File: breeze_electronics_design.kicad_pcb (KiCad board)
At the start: 2 copper layers, 104.1 x 104.1 mm, 104 parts, among them J1 SIP4, M1 MotorA, M2 MotorB, M3 MotorA, M4 MotorB, Q1 S8050, Q2 SI2302, Q3 SI2302, Q4 SI2302, Q5 SI2302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

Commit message: Finish the basic check of layout
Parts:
- removed the ? at (-94.9, -94.9)
- removed the ? at (-94.9, -5.08)
- removed the ? at (-5.08, -5.08)
- removed the ? at (-5.08, -94.9)
- added ?: , Footprint:PTH_Motor, F.Cu at (5.08, -94.9)
- added ?: Motor, Footprint:PTH_Motor, F.Cu at (94.9, -5.08)
- added ?: Motor, Footprint:PTH_Motor, F.Cu at (94.9, -94.9)
- added ?: Motor, Footprint:PTH_Motor, F.Cu at (5.08, -5.08)
- added REF**: LOGO_Arrow, Footprint:LOGO_Arrow, F.Cu at (50.0, -54.1)
- added REF**: LOGO_Project, Footprint:LOGO_Project, F.Cu at (64.5, -31.0)
- added REF***: OSHW-Logo_5.7x6mm_SilkScreen, Symbols:OSHW-Logo_5.7x6mm_SilkScreen, F.Cu at (57.4, -29.7)
- H1, LED3, LED5, LED7, LED9, M1, M2, M3, M4, USB1: moved to B.Cu
- S1: footprint Footprint:DIP_SW2x3 -> DIP_SW2x3
- moved C7 109.5 mm to (67.1, -43.4)
- moved LED6 102.6 mm to (77.5, -22.6)
- moved M4 101.6 mm to (81.3, -79.8)
- moved M1 101.5 mm to (20.3, -81.3)
- moved C6 100.6 mm to (55.4, -58.2)
- moved C9 100.6 mm to (55.4, -63.0)
- moved C4 100.3 mm to (69.3, -55.1)
- moved U5 100.3 mm to (58.9, -37.6)
- moved C16 100.3 mm to (36.8, -48.0)
- moved C3 100.3 mm to (50.0, -58.2)
- moved R14 100.3 mm to (30.5, -58.2)
- moved R2 100.3 mm to (50.0, -67.1)
- moved R3 100.3 mm to (50.0, -62.7)
- moved C24 100.1 mm to (27.4, -51.6)
- moved Y1 100.1 mm to (57.7, -51.6), turned to 270 degrees
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
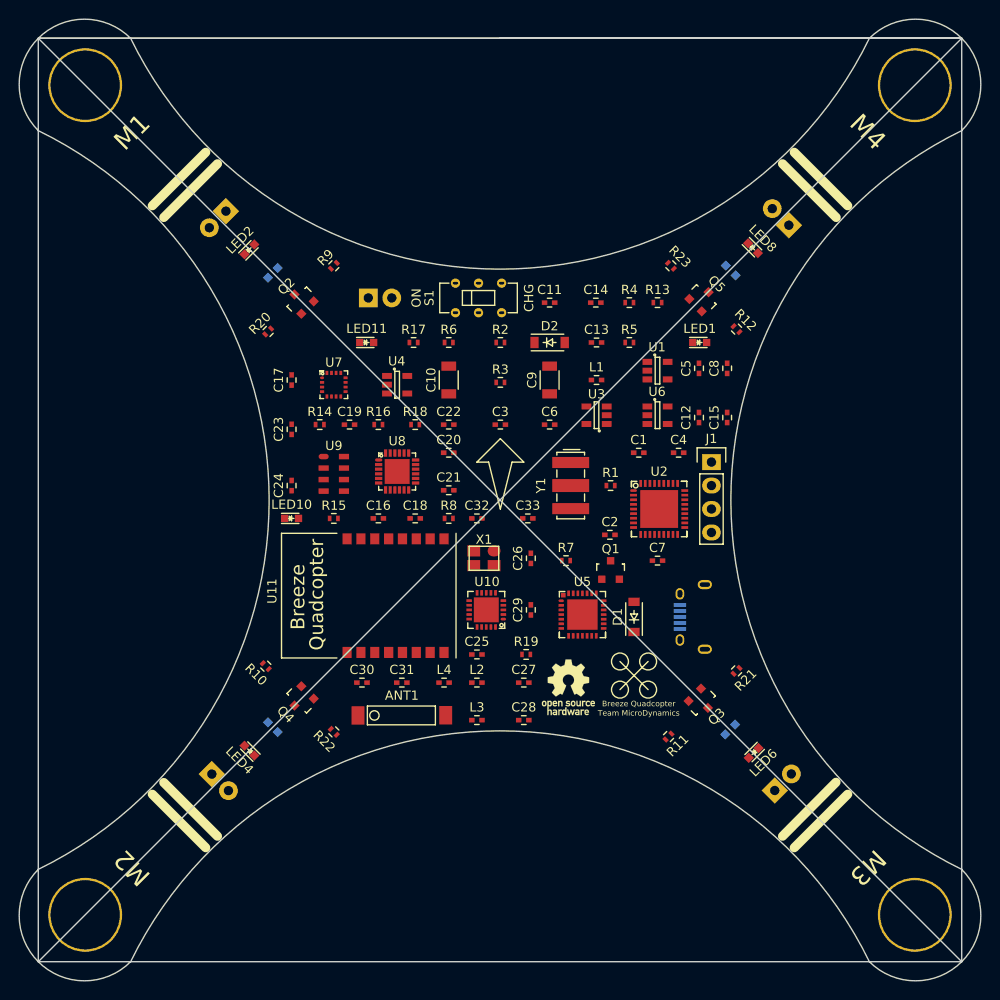
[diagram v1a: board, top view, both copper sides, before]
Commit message: Finish the basic wiring of LEDs
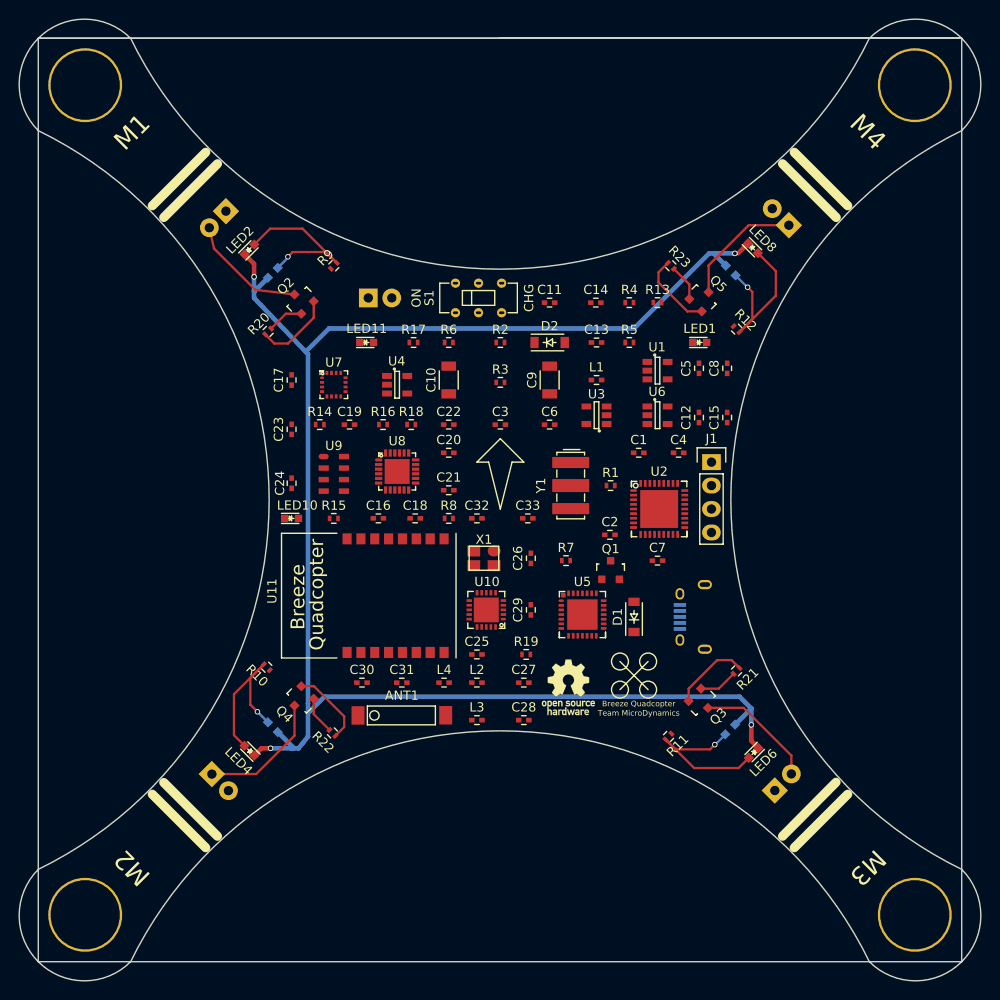
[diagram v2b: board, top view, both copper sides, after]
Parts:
- moved R16 0.51 mm to (37.3, -58.2)
- moved R18 0.43 mm to (40.4, -58.2)
- moved C24 0.25 mm to (27.4, -51.8), turned to 270 degrees
- moved R22 0.18 mm to (31.9, -24.8), turned to 315 degrees
- moved R10 0.16 mm to (24.7, -31.9)
- turned LED3 to 45 degrees
- turned LED5 to 135 degrees
- turned LED7 to 225 degrees
- turned LED9 to 315 degrees
- turned R20 to 225 degrees
- turned R21 to 45 degrees
- turned R23 to 135 degrees
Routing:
- net Net-(LED2-Pad1): track 0.00 -> 178.1 mm, vias 0 -> 4
- net Net-(LED2-Pad2): track 0.00 -> 18.9 mm, vias 0 -> 1
- net Net-(LED8-Pad2): track 0.00 -> 18.5 mm, vias 0 -> 1
- net Net-(LED6-Pad2): track 0.00 -> 18.3 mm, vias 0 -> 1
- net Net-(LED4-Pad2): track 0.00 -> 18.3 mm, vias 0 -> 1
- net Net-(M2-Pad1): track 0.00 -> 13.9 mm
- net Net-(M4-Pad1): track 0.00 -> 13.4 mm
- net Net-(M3-Pad2): track 0.00 -> 13.2 mm
- net Net-(M1-Pad2): track 0.00 -> 12.9 mm
- net Net-(Q2-Pad2): track 0.00 -> 8.60 mm
- net Net-(Q5-Pad2): track 0.00 -> 8.53 mm
- net Net-(Q4-Pad2): track 0.00 -> 8.49 mm
- net Net-(Q3-Pad2): track 0.00 -> 8.47 mm
- net /PWMC: track 0.00 -> 4.19 mm
- net /PWMB: track 0.00 -> 4.10 mm
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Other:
- net class Power added: clearance 0.2, trace_width 0.5, via_dia 0.6, via_drill 0.4
- net class Signal added: clearance 0.2, trace_width 0.25, via_dia 0.6, via_drill 0.4

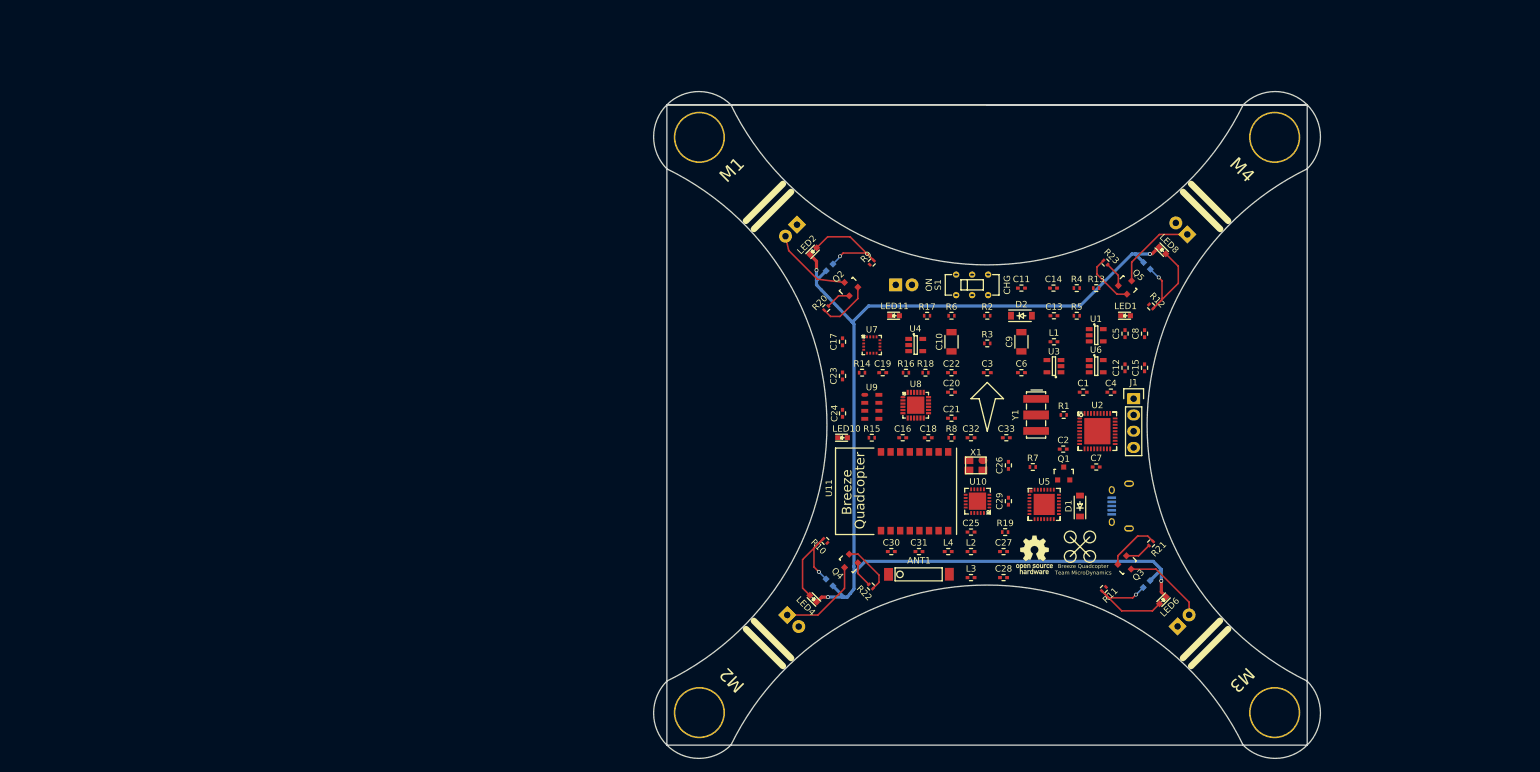
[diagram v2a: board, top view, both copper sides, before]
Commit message: Relocate the footprints of Wireless
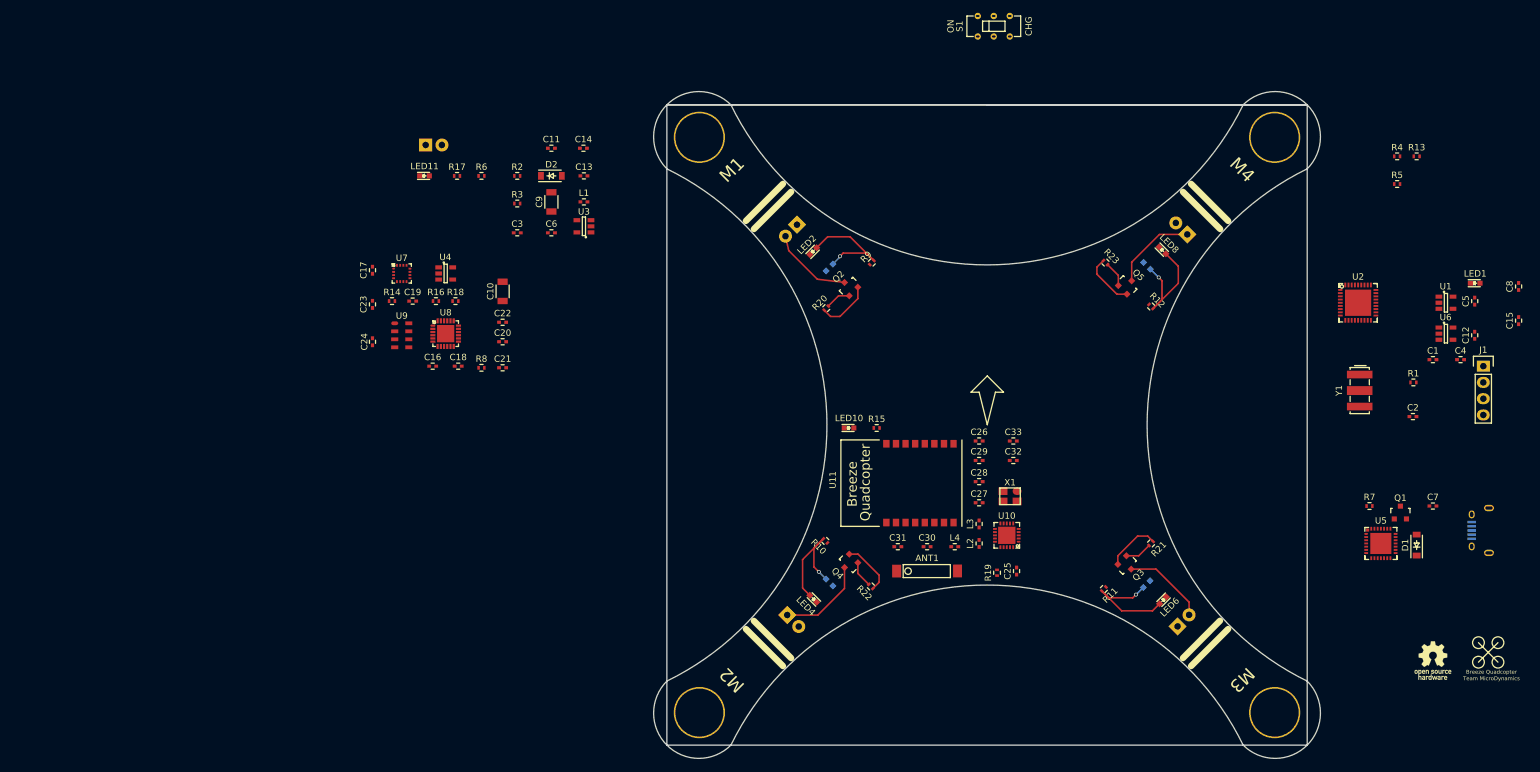
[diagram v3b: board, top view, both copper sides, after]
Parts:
- S1: footprint DIP_SW2x3 -> Footprint:DIP_SW2x3
- U11: footprint SMD_HM -> Footprint:SMD_HM
- moved C11 76.6 mm to (-18.0, -93.2)
- moved C13 76.6 mm to (-13.0, -88.9)
- moved C6 76.6 mm to (-18.0, -80.0)
- moved C9 76.6 mm to (-18.0, -84.8)
- moved D2 76.6 mm to (-18.0, -88.9)
- moved H1 76.6 mm to (-37.7, -93.7)
- moved L1 76.6 mm to (-13.0, -84.8)
- moved LED11 76.6 mm to (-37.8, -88.9)
- moved R17 76.6 mm to (-32.8, -88.9)
- moved R6 76.6 mm to (-29.0, -88.9)
- moved U3 76.6 mm to (-13.0, -81.0)
- moved C14 76.6 mm to (-13.0, -93.2)
- moved C3 76.6 mm to (-23.4, -80.0)
- moved R2 76.6 mm to (-23.4, -88.9)
- moved R3 76.6 mm to (-23.4, -84.6)
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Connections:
- U2 pad 36: /GND -> Net-(U2-Pad36)
- U2 pad 5: /GND -> Net-(U2-Pad5)
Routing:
- net Net-(LED2-Pad1): track 178.1 -> 0.40 mm, vias 4 -> 0
- net Net-(ANT1-Pad1): track 0.00 -> 0.53 mm
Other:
- net class Power removed

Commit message: Modify the footprints of Sensors
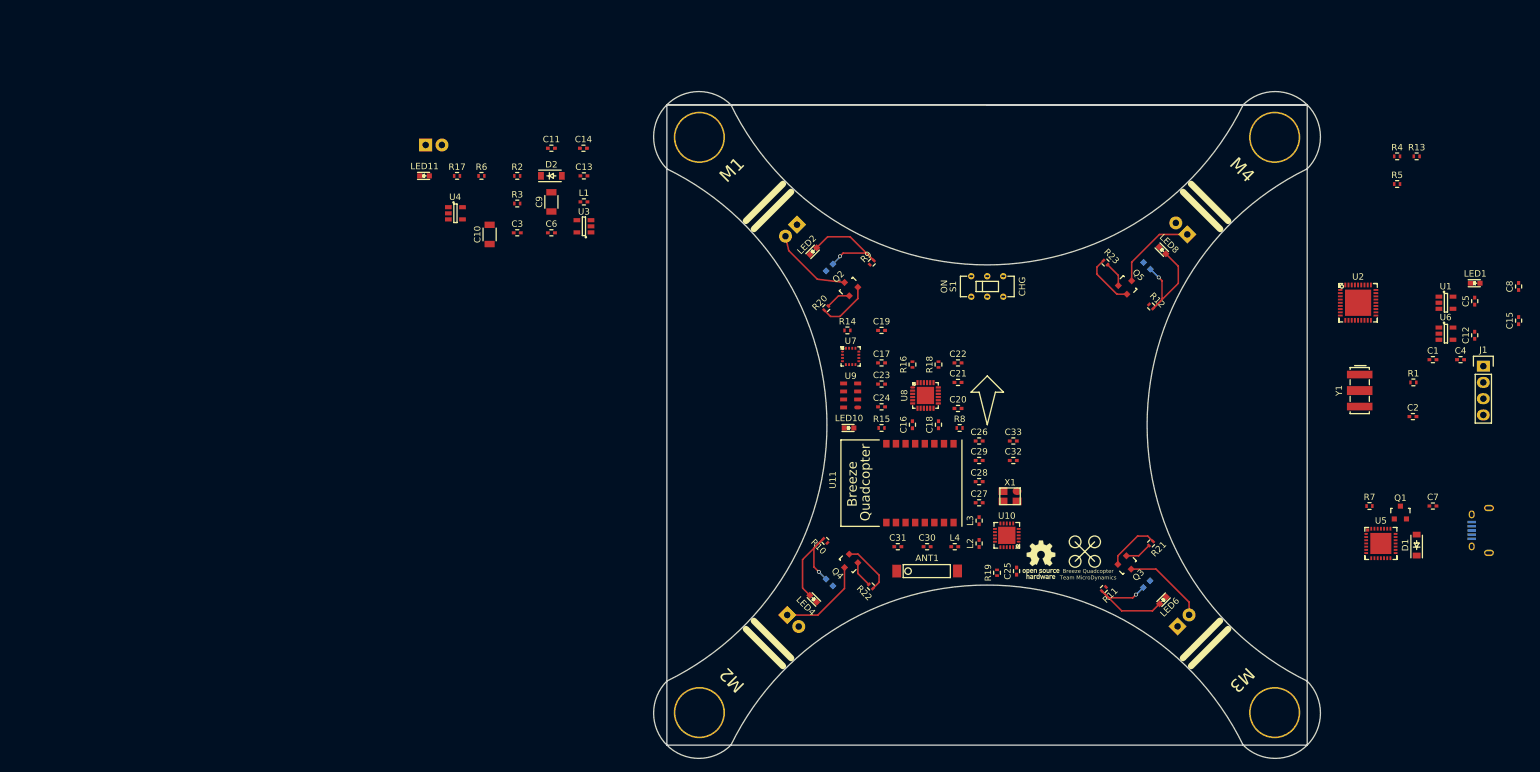
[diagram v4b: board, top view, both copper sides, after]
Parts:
- moved C17 80.8 mm to (33.5, -59.7), turned to 0 degrees
- moved C23 80.5 mm to (33.5, -56.4), turned to 0 degrees
- moved C24 80.1 mm to (33.5, -52.8), turned to 0 degrees
- moved R18 76.1 mm to (42.4, -59.4), turned to 270 degrees
- moved C18 75.6 mm to (42.4, -50.0), turned to 90 degrees
- moved U8 75.5 mm to (40.4, -54.6)
- moved C16 75.5 mm to (38.4, -50.0), turned to 270 degrees
- moved R8 75.3 mm to (45.7, -49.5)
- moved R16 75.1 mm to (38.4, -59.4), turned to 270 degrees
- moved C19 73.4 mm to (33.5, -64.8)
- moved C20 71.9 mm to (45.5, -52.6)
- moved C22 71.4 mm to (45.5, -59.7)
- moved U7 71.3 mm to (28.7, -60.7)
- moved R14 71.3 mm to (28.2, -64.8)
- moved C21 71.2 mm to (45.5, -56.6)
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
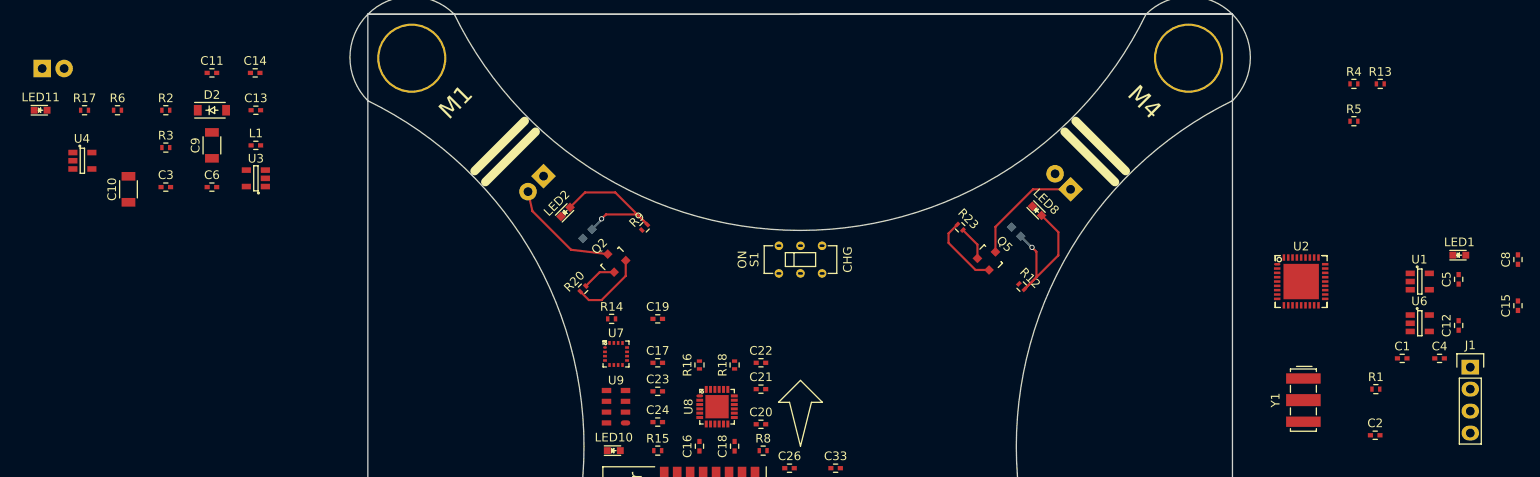
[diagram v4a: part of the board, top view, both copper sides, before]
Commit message: Relocate the footprints of Power
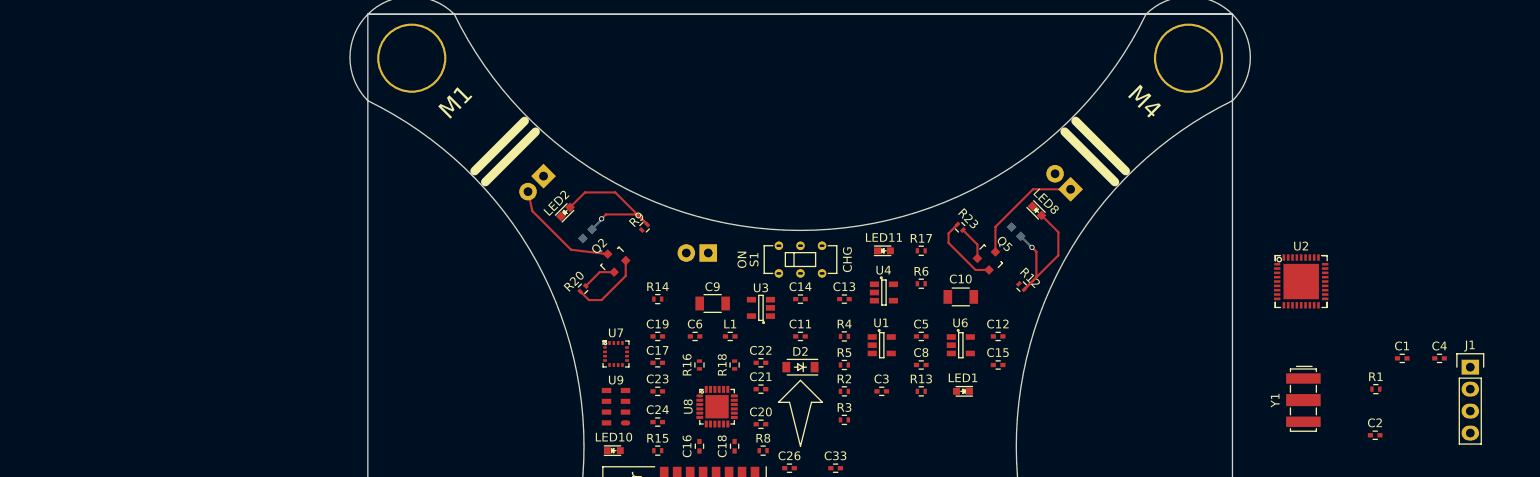
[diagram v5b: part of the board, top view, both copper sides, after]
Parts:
- moved LED11 98.9 mm to (59.7, -72.6)
- moved R17 98.1 mm to (64.0, -72.6)
- moved C10 97.1 mm to (68.6, -67.3), turned to 0 degrees
- moved R6 95.1 mm to (64.0, -68.8)
- moved U4 94.0 mm to (59.7, -67.8)
- moved C3 86.1 mm to (59.4, -56.4)
- moved R2 85.0 mm to (55.1, -56.4), turned to 180 degrees
- moved R3 84.6 mm to (55.1, -53.1), turned to 180 degrees
- moved H1 79.9 mm to (39.4, -72.4), turned to 90 degrees
- moved C11 74.6 mm to (50.0, -62.7), turned to 180 degrees
- moved D2 74.3 mm to (50.0, -59.2), turned to 180 degrees
- moved C13 71.5 mm to (55.1, -67.1)
- moved C8 70.1 mm to (64.0, -59.4), turned to 0 degrees
- moved C14 68.3 mm to (50.0, -67.1), turned to 180 degrees
- moved R4 65.8 mm to (55.1, -62.7)
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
